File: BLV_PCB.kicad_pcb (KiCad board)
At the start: 4 copper layers, 90 x 90 mm, 84 parts, among them J1 Cube0_UART_JST-PH, J10 USB_C_USB2.0_16P, J11 Micro_SD_Card, J12 RF SMA, J2 Cube0_UART_JST-PH, J3 Cube0_UART_JST-PH, J4 Cube0_UART_Debug, J5 Cube0_UART_Debug, J6 Cube0_UART_Debug, J7 Dupont Debug Headers, J8 USB_C_USB2.0_16P, Q1 Si2301CDS, Q2 Si2301CDS, SW1 SW_Push, SW2 SW_RUN, SW3 SW_Push, U1 W25Q128JVS, U2 RP2350_60QFN, U3 TPS63001DRCR, U4 BH-18650-A6AJ012, U5 E32-400M30S, U6 NEO-M9N, Y1 ABM8_262_T3

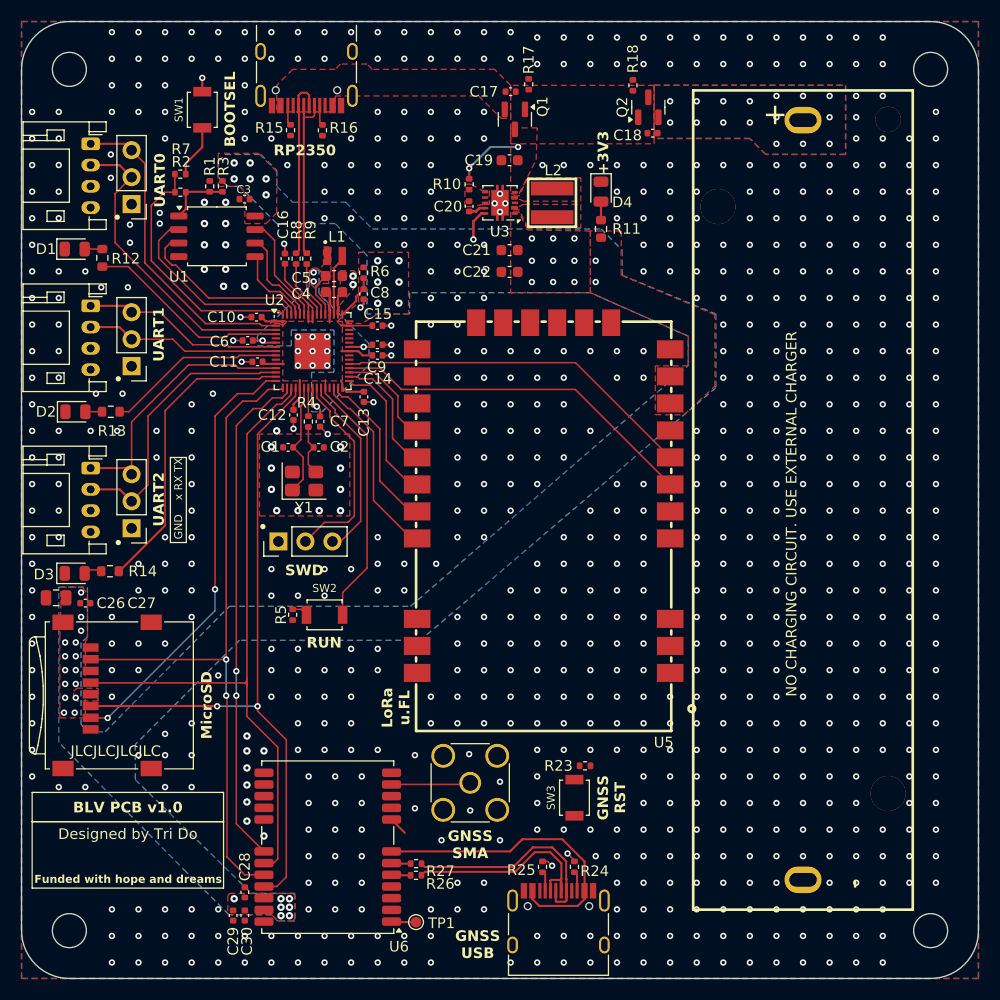
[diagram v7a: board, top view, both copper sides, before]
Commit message: General DFM fixes
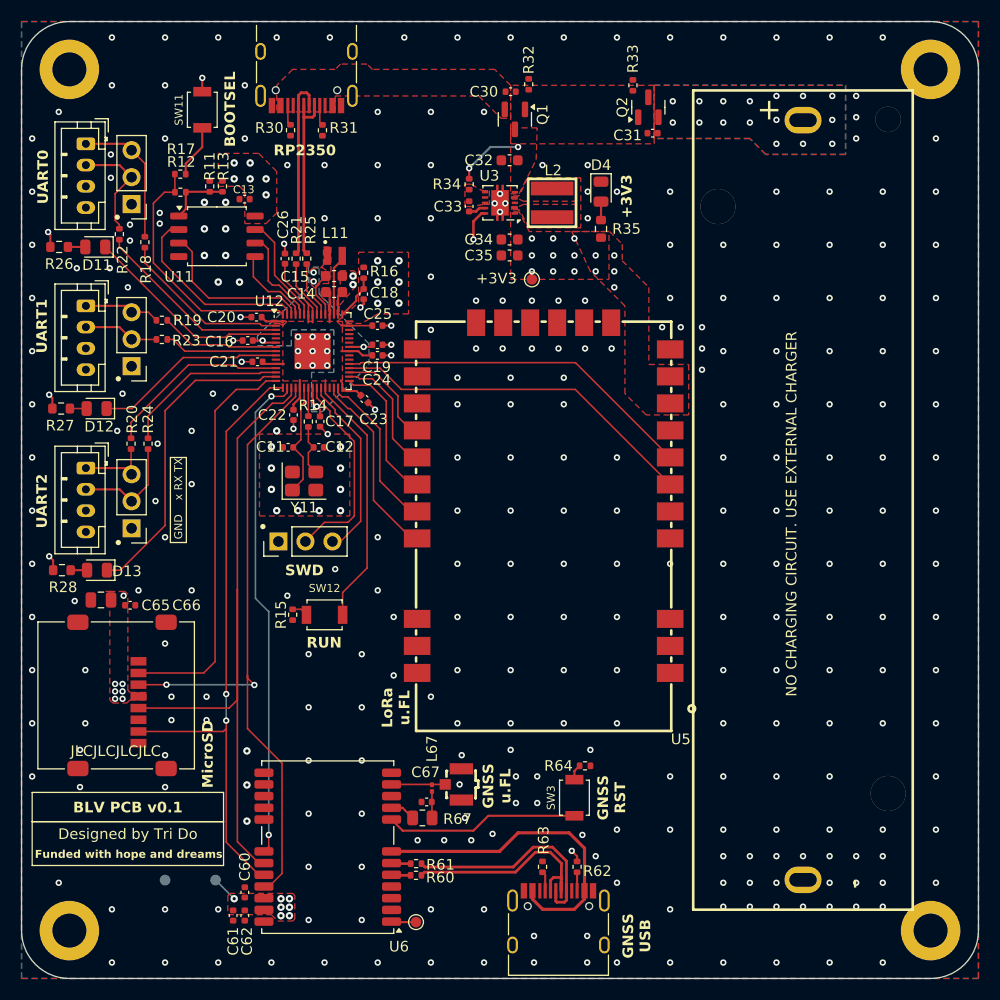
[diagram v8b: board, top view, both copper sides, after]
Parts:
- removed the J12 at (172.2, 111.6)
- added C67: 100n X7R, Capacitor_SMD:C_0402_1005Metric, F.Cu at (168.1, 113.4)
- added JP1: U.FL-R-SMT-1(80), easyeda2kicad:RF-SMD_FRF05002-JSS103M, F.Cu at (170.6, 111.8)
- added L67: 27n, Inductor_SMD:L_0201_0603Metric, F.Cu at (168.6, 112.1)
- added R18: 330, Resistor_SMD:R_0402_1005Metric, F.Cu at (141.6, 60.8)
- added R19: 330, Resistor_SMD:R_0402_1005Metric, F.Cu at (143.2, 68.1)
- added R20: 330, Resistor_SMD:R_0402_1005Metric, F.Cu at (140.3, 79.7)
- added R22: 330, Resistor_SMD:R_0402_1005Metric, F.Cu at (139.2, 60.0)
- added R23: 330, Resistor_SMD:R_0402_1005Metric, F.Cu at (143.2, 69.9)
- added R24: 330, Resistor_SMD:R_0402_1005Metric, F.Cu at (141.9, 79.7)
- added R67: 10, Resistor_SMD:R_0805_2012Metric, F.Cu at (167.7, 114.9)
- added TP2: +3V3, TestPoint:TestPoint_Pad_D1.0mm, B.Cu at (148.2, 120.8)
- added TP3: +3V3, TestPoint:TestPoint_Pad_D1.0mm, F.Cu at (178.0, 64.2)
- added TP4: GND, TestPoint:TestPoint_Pad_D1.0mm, B.Cu at (143.5, 120.8)
- C14: renamed from C4; value 4u7 -> 4.7u
- C15: renamed from C5; value 4u7 -> 4.7u
- C17: renamed from C7; value 4u7 -> 4.7u
- C18: renamed from C8; value 4u7 -> 4.7u
- C62: renamed from C30; value 100nF -> 100n
- H1, H2, H3, H4: footprint MountingHole:MountingHole_3.2mm_M3 -> MountingHole:MountingHole_3.2mm_M3_DIN965_Pad
- J1, J2, J3: value Cube0_UART_JST-PH -> JST-PH; footprint Connector_JST:JST_PH_S4B-PH-K_1x04_P2.00mm_Horizontal -> Connector_JST:JST_PH_B4B-PH-K_1x04_P2.00mm_Vertical
- J11: footprint Connector_Card:microSD_HC_Wuerth_693072010801 -> Connector_Card:microSD_HC_Molex_47219-2001
- J12: renamed from J7; value Dupont Debug Headers -> duPont
- J4, J5, J6: value Cube0_UART_Debug -> duPont
- R26: renamed from R12; value 1k -> 470
- R27: renamed from R13; value 1k -> 470
- R28: renamed from R14; value 1k -> 470
- R30: renamed from R15; value 5k1 -> 5.1k
- R31: renamed from R16; value 5k1 -> 5.1k
- R62: renamed from R24; value 5k1 -> 5.1k
- R63: renamed from R25; value 5k1 -> 5.1k
- SW11: renamed from SW1; value SW_Push -> SW_QSPI
- SW3: value SW_Push -> SW_GNSS
- TP1: value TestPoint -> nSAFEBOOT
- moved R27 4.68 mm to (133.7, 76.4), turned to 0 degrees
- moved R28 4.53 mm to (133.8, 91.6), turned to 0 degrees
- moved C65 4.22 mm to (137.5, 94.4)
- moved C66 4.22 mm to (140.2, 94.9)
- moved R26 4.19 mm to (133.5, 61.2), turned to 0 degrees
- moved D13 2.12 mm to (137.1, 91.6), turned to 180 degrees
- moved D12 2.02 mm to (137.1, 76.4), turned to 180 degrees
- moved D11 1.95 mm to (136.9, 61.2), turned to 180 degrees
- moved C35 1.55 mm to (175.9, 62.0)
- moved C34 1.00 mm to (175.9, 60.5)
- moved J11 0.85 mm to (138.9, 103.4), turned to -90 degrees
- moved J1 0.45 mm to (136.1, 51.5)
- moved J2 0.45 mm to (136.1, 66.7)
- moved J3 0.45 mm to (136.1, 82.0)
- moved R62 0.25 mm to (182.2, 119.5)
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- renumbered C1 to C11, C2 to C12, C3 to C13, C6 to C16, C9 to C19, C10 to C20, C11 to C21, C12 to C22, C13 to C23, C14 to C24, C15 to C25, C16 to C26, C17 to C30, C18 to C31, C19 to C32, C20 to C33, C21 to C34, C22 to C35, C28 to C60, C29 to C61, C26 to C65, C27 to C66, D1 to D11, D2 to D12, D3 to D13, L1 to L11, R1 to R11, R2 to R12, R3 to R13, R4 to R14, R5 to R15, R6 to R16, R7 to R17, R8 to R21, R9 to R25, R17 to R32, R18 to R33, R10 to R34, R11 to R35, R26 to R60, R27 to R61, R23 to R64, SW2 to SW12, U1 to U11, U2 to U12, Y1 to Y11
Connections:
- D11 pad 1: GND -> /MCU/Cube0_LED
- D12 pad 1: GND -> /MCU/Cube1_LED
- D13 pad 1: GND -> /MCU/Cube2_LED
- R26 pad 1: /MCU/Cube0_LED -> +3V3
- R27 pad 1: /MCU/Cube1_LED -> +3V3
- R28 pad 1: /MCU/Cube2_LED -> +3V3
- U12 pad 12: /Cube2_UART_TX -> Net-(U12-GPIO8)
- U12 pad 13: /Cube2_UART_RX -> Net-(U12-GPIO9)
- U12 pad 2: /Cube0_UART_TX -> Net-(U12-GPIO0)
- U12 pad 3: /Cube0_UART_RX -> Net-(U12-GPIO1)
- U12 pad 7: /Cube1_UART_TX -> Net-(U12-GPIO4)
- U12 pad 8: /Cube1_UART_RX -> Net-(U12-GPIO5)
- U6 pad 9: unconnected-(U6-VCC_RF-Pad9) -> /GNSS & MicroSD/VCC_RF
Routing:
- net /Cube0_UART_RX: track 29.7 -> 9.98 mm
- net Net-(U12-GPIO1): track 0.00 -> 18.7 mm
- net /Cube2_UART_TX: track 24.9 -> 6.48 mm
- net Net-(U12-GPIO8): track 0.00 -> 17.5 mm
- net /Cube0_UART_TX: track 30.0 -> 12.8 mm
- net /Cube2_UART_RX: track 26.7 -> 9.87 mm
- net /GNSS & MicroSD/GNSS_RST: track 1.77 -> 18.2 mm
- net Net-(U12-GPIO0): track 0.00 -> 16.2 mm
- net Net-(U12-GPIO9): track 0.00 -> 15.8 mm
- net /Cube1_UART_TX: track 19.0 -> 6.75 mm
- net /Cube1_UART_RX: track 18.4 -> 6.70 mm
- net Net-(U12-GPIO4): track 0.00 -> 11.3 mm
- net Net-(U12-GPIO5): track 0.00 -> 10.7 mm
- net +3V3: track 55.4 -> 62.1 mm, vias 46 -> 44
- net /GNSS & MicroSD/SPI_MISO: track 64.8 -> 58.8 mm
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- added copper zone on In2.Cu, net +3V3
- removed copper zone on B.Cu, net +3V3
- removed copper zone on In2.Cu, net GND
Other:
- board text added: "BLV PCB v0.1"
- board text added: "GND"
- board text added: "GNSS u.FL"
- board text removed: "BLV PCB v1.0"
- board text removed: "GNSS SMA"
- board text removed: "We can't even afford Double-Sided PCBA"
